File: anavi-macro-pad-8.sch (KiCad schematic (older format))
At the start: 41 parts, among them J1 USB_B_Micro, J2 Conn_01x04_Female, J3 Conn_01x03_Male, J4 Conn_01x03_Male, Q1 Q_NPN_BEC, SW1 SW_DIP_x01, SW2 SW_DIP_x01, SW3 SW_DIP_x01, SW4 SW_DIP_x01, SW5 SW_DIP_x01, SW6 SW_DIP_x01, SW7 SW_DIP_x01, SW8 SW_DIP_x01, U1 ATmega32U4-AU, Y1 Crystal

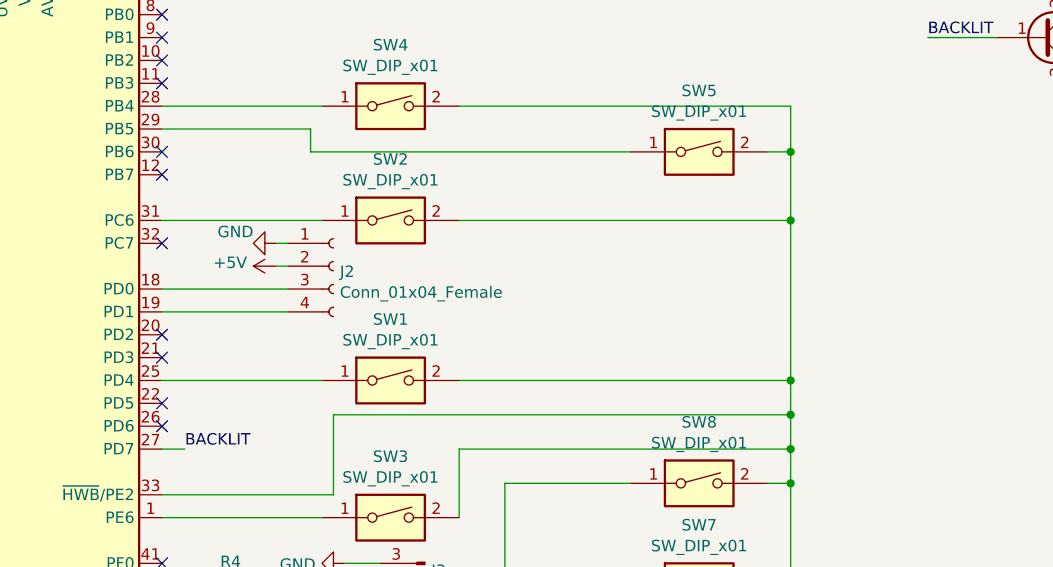
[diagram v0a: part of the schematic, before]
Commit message: Add outline and arrange components
Signed-off-by: Leon Anavi <leon@anavi.org>
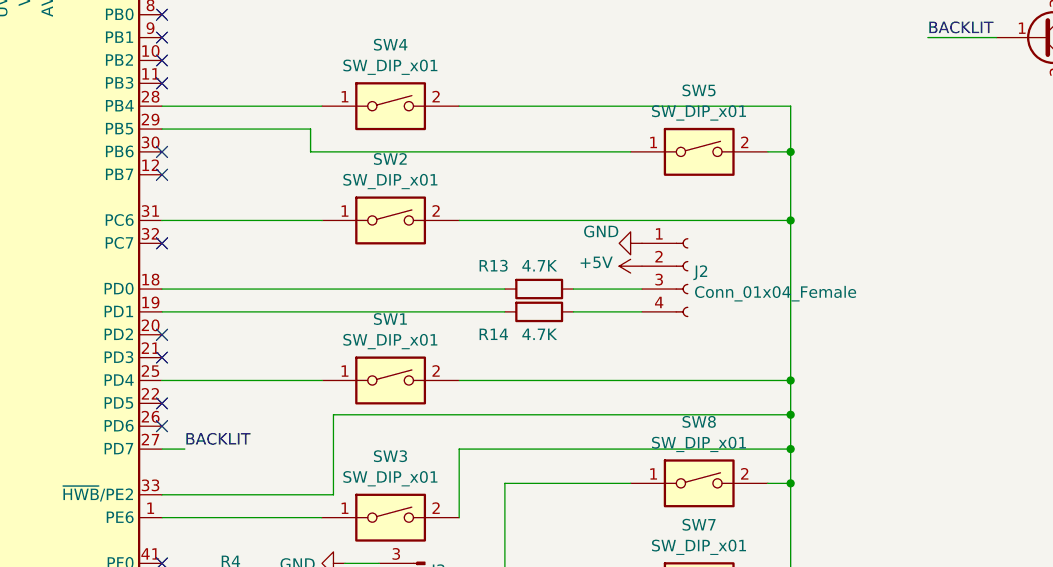
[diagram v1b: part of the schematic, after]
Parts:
- added R13, R14: 4.7K, Resistors_SMD:R_0603, symbol Device:R
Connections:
- net at J2.3 (Pin_3): now also R13.1; no longer U1.18 (PD0)
- net at J2.4 (Pin_4): now also R14.1; no longer U1.19 (PD1)
- new net: R13.2, U1.18 (PD0)
- new net: R14.2, U1.19 (PD1)
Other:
- moved on the sheet: J2
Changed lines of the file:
@@
 L Connector:Conn_01x04_Female J2
 U 1 1 5EC82683
-P 5700 3400
-F 0 "J2" H 5728 3376 50  0000 L CNN
-F 1 "Conn_01x04_Female" H 5728 3285 50  0000 L CNN
-F 2 "Connector_PinHeader_2.54mm:PinHeader_1x04_P2.54mm_Vertical" H 5700 3400 50  0001 C CNN
-F 3 "~" H 5700 3400 50  0001 C CNN
-	1    5700 3400
+P 7250 3400
+F 0 "J2" H 7278 3376 50  0000 L CNN
+F 1 "Conn_01x04_Female" H 7278 3285 50  0000 L CNN
+F 2 "Connector_PinHeader_2.54mm:PinHeader_1x04_P2.54mm_Vertical" H 7250 3400 50  0001 C CNN
+F 3 "~" H 7250 3400 50  0001 C CNN
+	1    7250 3400
 	1    0    0    -1
 $EndComp
@@
 L power:GND #PWR0113
 U 1 1 5EC8926C
-P 5450 3300
-F 0 "#PWR0113" H 5450 3050 50  0001 C CNN
-F 1 "GND" V 5400 3200 50  0000 R CNN
-F 2 "" H 5450 3300 50  0001 C CNN
-F 3 "" H 5450 3300 50  0001 C CNN
-	1    5450 3300
+P 7050 3300
+F 0 "#PWR0113" H 7050 3050 50  0001 C CNN
+F 1 "GND" V 7000 3200 50  0000 R CNN
+F 2 "" H 7050 3300 50  0001 C CNN
+F 3 "" H 7050 3300 50  0001 C CNN
+	1    7050 3300
 	0    1    1    0
 $EndComp
@@
 L power:+5V #PWR0114
 U 1 1 5EC8C111
-P 5450 3400
-F 0 "#PWR0114" H 5450 3250 50  0001 C CNN
-F 1 "+5V" V 5465 3528 50  0000 L CNN
-F 2 "" H 5450 3400 50  0001 C CNN
-F 3 "" H 5450 3400 50  0001 C CNN
-	1    5450 3400
-	0    -1   -1   0
-$EndComp
-Wire Wire Line
-	5450 3300 5500 3300
-Wire Wire Line
-	5450 3400 5500 3400
-Wire Wire Line
-	4950 3500 5500 3500
-Wire Wire Line
-	4950 3600 5500 3600
+P 7050 3400
+F 0 "#PWR0114" H 7050 3250 50  0001 C CNN
+F 1 "+5V" V 7065 3528 50  0000 L CNN
+F 2 "" H 7050 3400 50  0001 C CNN
+F 3 "" H 7050 3400 50  0001 C CNN
+	1    7050 3400
+	0    -1   -1   0
+$EndComp
 $Comp
 L Device:R R4
@@
 Wire Wire Line
 	8900 5050 8900 5400
+$Comp
+L Device:R R13
+U 1 1 5EAF8E5F
+P 6600 3500
+F 0 "R13" V 6500 3300 50  0000 C CNN
+F 1 "4.7K" V 6500 3500 50  0000 C CNN
+F 2 "Resistors_SMD:R_0603" V 6530 3500 50  0001 C CNN
+F 3 "~" H 6600 3500 50  0001 C CNN
+	1    6600 3500
+	0    1    1    0
+$EndComp
+$Comp
+L Device:R R14
+U 1 1 5EAF97BA
+P 6600 3600
+F 0 "R14" V 6700 3400 50  0000 C CNN
+F 1 "4.7K" V 6700 3600 50  0000 C CNN
+F 2 "Resistors_SMD:R_0603" V 6530 3600 50  0001 C CNN
+F 3 "~" H 6600 3600 50  0001 C CNN
+	1    6600 3600
+	0    1    1    0
+$EndComp
+Wire Wire Line
+	6750 3500 7050 3500
+Wire Wire Line
+	6750 3600 7050 3600
+Wire Wire Line
+	4950 3500 6450 3500
+Wire Wire Line
+	4950 3600 6450 3600
 $EndSCHEMATC

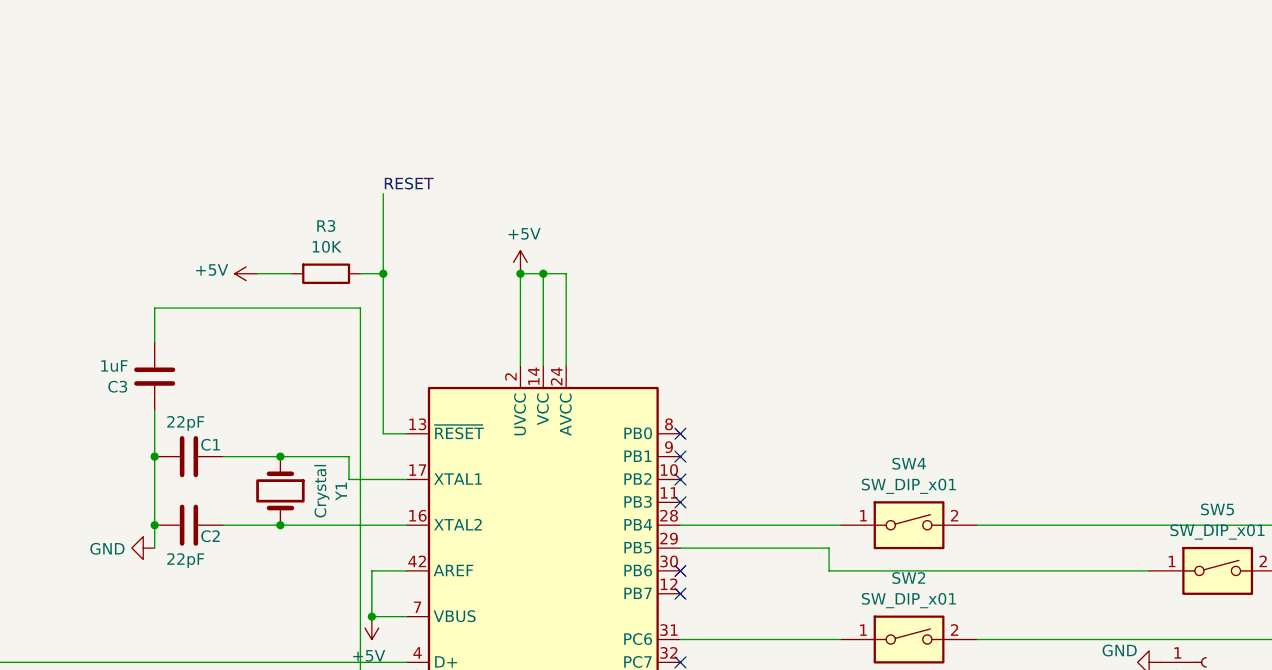
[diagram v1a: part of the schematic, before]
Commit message: Add components to the schematics
The following modificaitons to the schematics and the PCB have
been done:

* Added RESET button
* Added pins for AVR SPI programmer
* Changed the crystal footprint to 3225
* Minor modificaitons to the PCB layouts

Signed-off-by: Leon Anavi <leon@anavi.org>
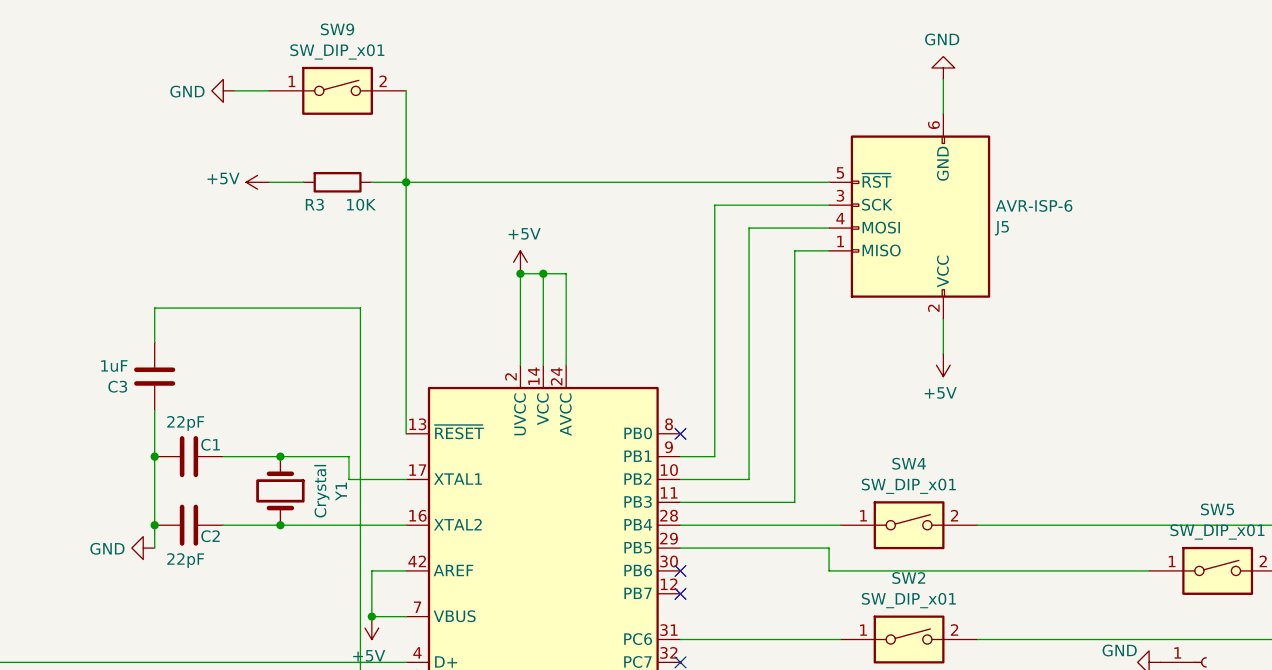
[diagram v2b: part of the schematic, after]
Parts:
- added J5: AVR-ISP-6, Connector_PinHeader_2.54mm:PinHeader_2x03_P2.54mm_Vertical, symbol Connector:AVR-ISP-6
- added SW9: SW_DIP_x01, Buttons_Switches_ThroughHole:SW_PUSH_6mm_h4.3mm, symbol Switch:SW_DIP_x01
- Y1: footprint Crystals:Crystal_HC49-SD_SMD -> anavi-macro-pad-8:Crystal_SMD_3225-4Pin_3.2x2.5mm_HandSoldering
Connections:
- net +5V: now also J5.2 (VCC)
- net GND: now also J5.6 (GND), SW9.1
- net at U1.10 (PB2): now also J5.4 (MOSI)
- net at U1.11 (PB3): now also J5.1 (MISO)
- net at U1.9 (PB1): now also J5.3 (SCK)
- net RESET: no longer names the net of R3.1, U1.13 (~RESET)
- net RESET: now also J5.5 (~RST), SW9.2
- no-connect marks 15 -> 12
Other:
- moved on the sheet: R3
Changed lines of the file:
@@
 F 0 "Y1" H 3200 2818 50  0000 C CNN
 F 1 "Crystal" H 3200 2727 50  0000 C CNN
-F 2 "Crystals:Crystal_HC49-SD_SMD" H 3200 2550 50  0001 C CNN
+F 2 "anavi-macro-pad-8:Crystal_SMD_3225-4Pin_3.2x2.5mm_HandSoldering" H 3200 2550 50  0001 C CNN
 F 3 "~" H 3200 2550 50  0001 C CNN
 	1    3200 2550
@@
 	1    0    0    -1
 $EndComp
-Wire Wire Line
-	3650 2300 3750 2300
-Text Label 3650 1250 0    50   ~ 0
-RESET
 $Comp
 L power:+5V #PWR0106
 U 1 1 5EB3E276
-P 3100 1600
-F 0 "#PWR0106" H 3100 1450 50  0001 C CNN
-F 1 "+5V" V 3115 1728 50  0000 L CNN
-F 2 "" H 3100 1600 50  0001 C CNN
-F 3 "" H 3100 1600 50  0001 C CNN
-	1    3100 1600
-	0    -1   -1   0
-$EndComp
-Wire Wire Line
-	3250 1600 3100 1600
-Wire Wire Line
-	3550 1600 3650 1600
-Wire Wire Line
-	3650 1600 3650 1250
+P 3150 1200
+F 0 "#PWR0106" H 3150 1050 50  0001 C CNN
+F 1 "+5V" V 3165 1328 50  0000 L CNN
+F 2 "" H 3150 1200 50  0001 C CNN
+F 3 "" H 3150 1200 50  0001 C CNN
+	1    3150 1200
+	0    -1   -1   0
+$EndComp
+Wire Wire Line
+	3300 1200 3150 1200
 Wire Wire Line
 	2650 2200 2650 2400
@@
 	2650 1900 2650 1750
 Wire Wire Line
-	3650 2300 3650 1600
-Connection ~ 3650 1600
-Wire Wire Line
 	2650 1750 3550 1750
 $Comp
 L Device:R R3
 U 1 1 5EB39830
-P 3400 1600
-F 0 "R3" V 3193 1600 50  0000 C CNN
-F 1 "10K" V 3284 1600 50  0000 C CNN
-F 2 "Resistors_SMD:R_0603" V 3330 1600 50  0001 C CNN
-F 3 "~" H 3400 1600 50  0001 C CNN
-	1    3400 1600
+P 3450 1200
+F 0 "R3" V 3550 1100 50  0000 C CNN
+F 1 "10K" V 3550 1300 50  0000 C CNN
+F 2 "Resistors_SMD:R_0603" V 3380 1200 50  0001 C CNN
+F 3 "~" H 3450 1200 50  0001 C CNN
+	1    3450 1200
 	0    1    1    0
 $EndComp
@@
 	3550 3600 3750 3600
 NoConn ~ 4950 2300
-NoConn ~ 4950 2400
-NoConn ~ 4950 2500
-NoConn ~ 4950 2600
 NoConn ~ 4950 2900
 NoConn ~ 4950 3000
@@
 Wire Wire Line
 	4950 3600 6450 3600
+$Comp
+L Connector:AVR-ISP-6 J5
+U 1 1 5EB32D30
+P 6000 1300
+F 0 "J5" H 5671 1396 50  0000 R CNN
+F 1 "AVR-ISP-6" H 5671 1305 50  0000 R CNN
+F 2 "Connector_PinHeader_2.54mm:PinHeader_2x03_P2.54mm_Vertical" V 5750 1350 50  0001 C CNN
+F 3 " ~" H 4725 750 50  0001 C CNN
+	1    6000 1300
+	-1   0    0    1
+$EndComp
+$Comp
+L power:GND #PWR0121
+U 1 1 5EB3A3FA
+P 6100 750
+F 0 "#PWR0121" H 6100 500 50  0001 C CNN
+F 1 "GND" H 6105 577 50  0000 C CNN
+F 2 "" H 6100 750 50  0001 C CNN
+F 3 "" H 6100 750 50  0001 C CNN
+	1    6100 750
+	-1   0    0    1
+$EndComp
+$Comp
+L power:+5V #PWR0122
+U 1 1 5EB3A913
+P 6100 1950
+F 0 "#PWR0122" H 6100 1800 50  0001 C CNN
+F 1 "+5V" H 6115 2123 50  0000 C CNN
+F 2 "" H 6100 1950 50  0001 C CNN
+F 3 "" H 6100 1950 50  0001 C CNN
+	1    6100 1950
+	-1   0    0    1
+$EndComp
+Wire Wire Line
+	6100 1800 6100 1950
+Wire Wire Line
+	6100 750  6100 900
+Wire Wire Line
+	4950 2400 5100 2400
+Wire Wire Line
+	5100 2400 5100 1300
+Wire Wire Line
+	5100 1300 5600 1300
+Wire Wire Line
+	4950 2600 5450 2600
+Wire Wire Line
+	5450 2600 5450 1500
+Wire Wire Line
+	5450 1500 5600 1500
+Wire Wire Line
+	4950 2500 5250 2500
+Wire Wire Line
+	5250 2500 5250 1400
+Wire Wire Line
+	5250 1400 5600 1400
+$Comp
+L Switch:SW_DIP_x01 SW9
+U 1 1 5EB8BCC9
+P 3450 800
+F 0 "SW9" H 3450 1067 50  0000 C CNN
+F 1 "SW_DIP_x01" H 3450 976 50  0000 C CNN
+F 2 "Buttons_Switches_ThroughHole:SW_PUSH_6mm_h4.3mm" H 3450 800 50  0001 C CNN
+F 3 "~" H 3450 800 50  0001 C CNN
+	1    3450 800
+	1    0    0    -1
+$EndComp
+$Comp
+L power:GND #PWR0123
+U 1 1 5EB99916
+P 3000 800
+F 0 "#PWR0123" H 3000 550 50  0001 C CNN
+F 1 "GND" V 3005 672 50  0000 R CNN
+F 2 "" H 3000 800 50  0001 C CNN
+F 3 "" H 3000 800 50  0001 C CNN
+	1    3000 800
+	0    1    1    0
+$EndComp
+Wire Wire Line
+	3150 800  3000 800
+Wire Wire Line
+	5600 1200 3750 1200
+Wire Wire Line
+	3750 2300 3750 1200
+Wire Wire Line
+	3600 1200 3750 1200
+Connection ~ 3750 1200
+Wire Wire Line
+	3750 1200 3750 800
 $EndSCHEMATC

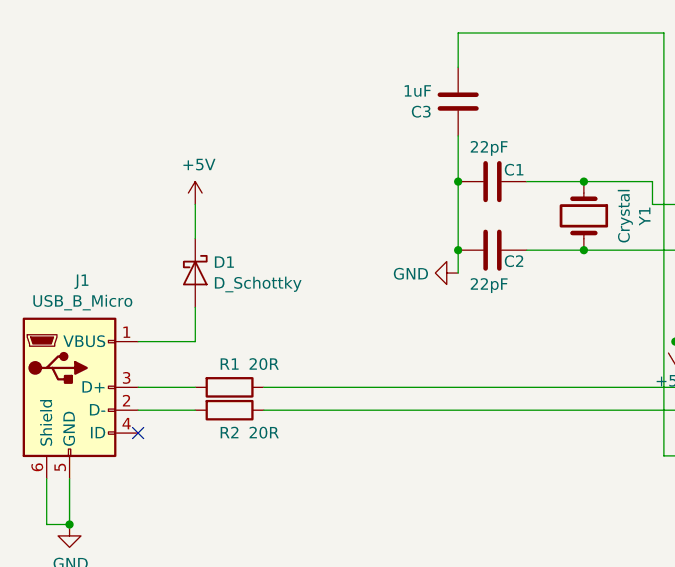
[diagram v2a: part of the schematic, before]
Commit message: anavi-macro-pad-8: Routing with Schottky diode
Add appropriate footprint for Schottky diode and complete the
routing of the PCB.

Signed-off-by: Leon Anavi <leon@anavi.org>
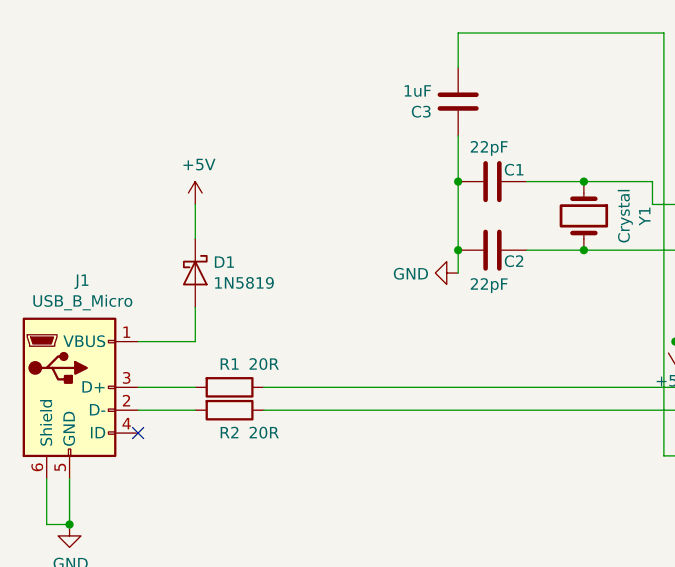
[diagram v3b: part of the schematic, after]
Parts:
- D1: value D_Schottky -> 1N5819; footprint (none) -> Diodes_SMD:SMA_Standard
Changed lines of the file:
@@
 P 1500 2800
 F 0 "D1" V 1454 2879 50  0000 L CNN
-F 1 "D_Schottky" V 1545 2879 50  0000 L CNN
-F 2 "" H 1500 2800 50  0001 C CNN
+F 1 "1N5819" V 1545 2879 50  0000 L CNN
+F 2 "Diodes_SMD:SMA_Standard" H 1500 2800 50  0001 C CNN
 F 3 "~" H 1500 2800 50  0001 C CNN
 	1    1500 2800
